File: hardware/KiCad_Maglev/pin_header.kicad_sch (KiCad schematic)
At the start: 0 parts

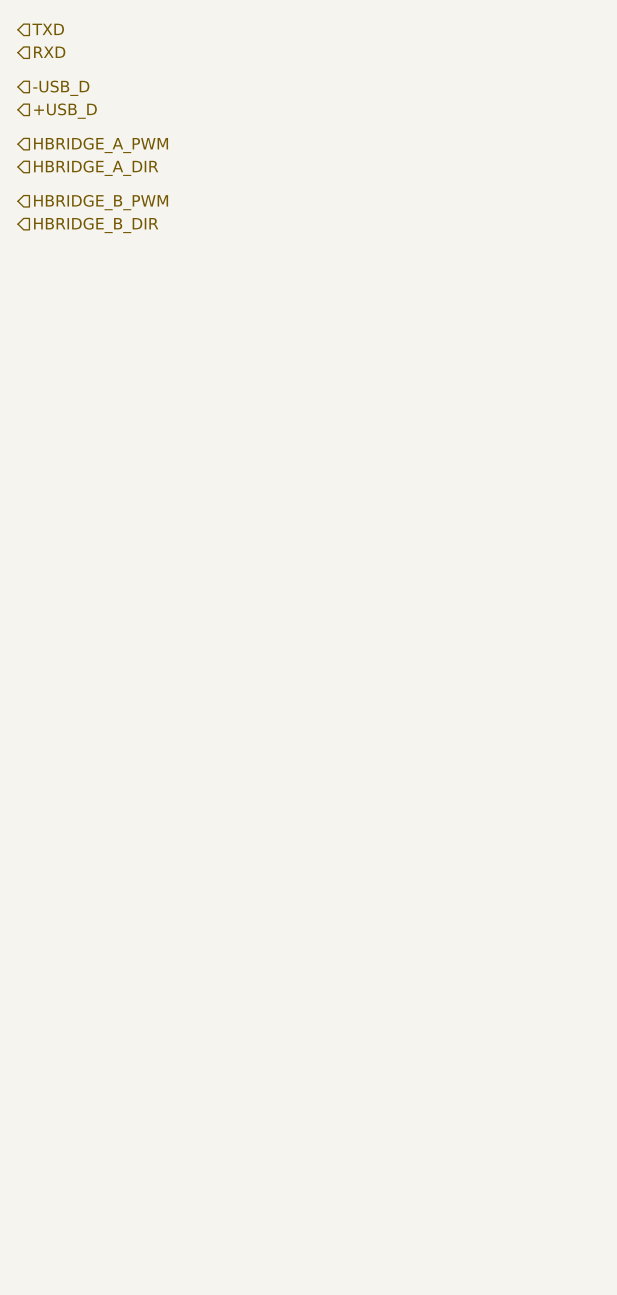
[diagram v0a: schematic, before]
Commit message: Update KiCad schematic sheets
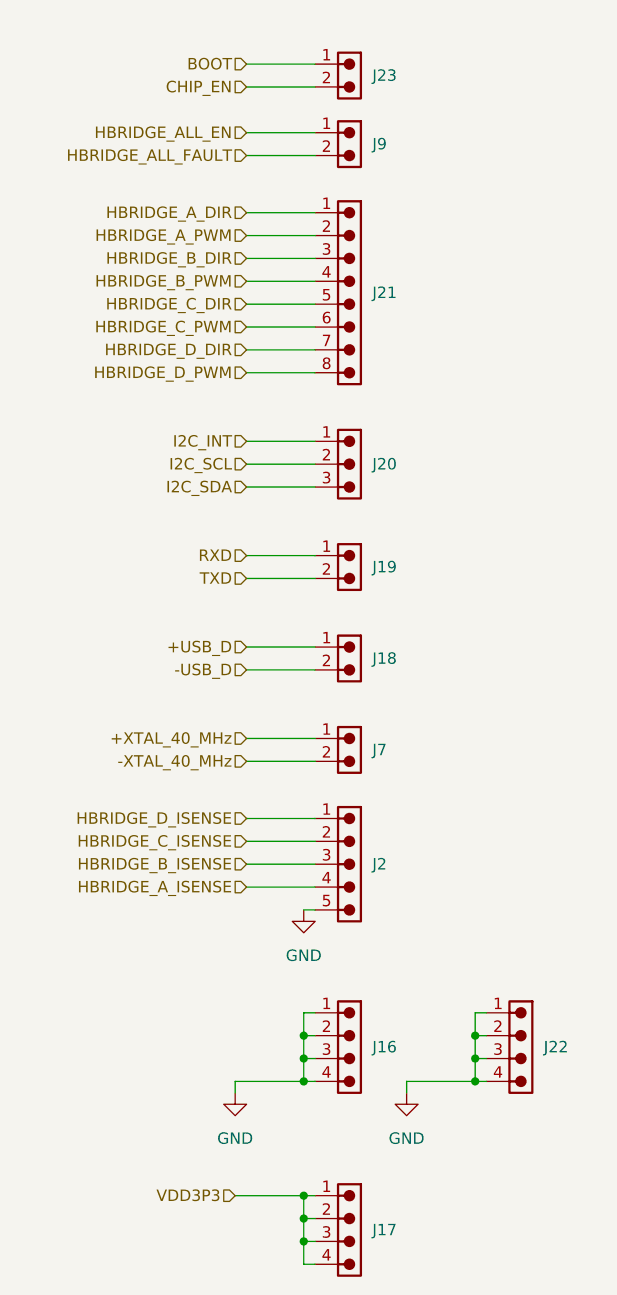
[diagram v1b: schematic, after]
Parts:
- added J16, J17, J22: 61300411121, Connector_THT_Wurth:J_Wurth_WR-PHD_61300411121, symbol Connector_Wurth_WR-PHD:61300411121
- added J18, J19, J23, J7, J9: 61300211121, Connector_THT_Wurth:J_Wurth_WR-PHD_61300211121, symbol Connector_Wurth_WR-PHD:61300211121
- added J2: 61300511121, Connector_THT_Wurth:J_Wurth_WR-PHD_61300511121, symbol Connector_Wurth_WR-PHD:61300511121
- added J20: 61300311121, Connector_THT_Wurth:J_Wurth_WR-PHD_61300311121, symbol Connector_Wurth_WR-PHD:61300311121
- added J21: 61300811121, Connector_THT_Wurth:J_Wurth_WR-PHD_61300811121, symbol Connector_Wurth_WR-PHD:61300811121
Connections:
- net +USB_D: now also J18.1
- net -USB_D: now also J18.2
- net HBRIDGE_A_DIR: now also J21.1
- net HBRIDGE_A_PWM: now also J21.2
- net HBRIDGE_B_DIR: now also J21.3
- net HBRIDGE_B_PWM: now also J21.4
- net RXD: now also J19.1
- net TXD: now also J19.2
- new net +XTAL_40_MHz: J7.1
- new net -XTAL_40_MHz: J7.2
- new net BOOT: J23.1
- new net CHIP_EN: J23.2
- new net GND: J16.1, J16.2, J16.3, J16.4, J2.5, J22.1, J22.2, J22.3, J22.4
- new net HBRIDGE_ALL_EN: J9.1
- new net HBRIDGE_ALL_FAULT: J9.2
- new net HBRIDGE_A_ISENSE: J2.4
- new net HBRIDGE_B_ISENSE: J2.3
- new net HBRIDGE_C_DIR: J21.5
- new net HBRIDGE_C_ISENSE: J2.2
- new net HBRIDGE_C_PWM: J21.6
- new net HBRIDGE_D_DIR: J21.7
- new net HBRIDGE_D_ISENSE: J2.1
- new net HBRIDGE_D_PWM: J21.8
- new net I2C_INT: J20.1
- new net I2C_SCL: J20.2
- new net I2C_SDA: J20.3
- new net VDD3P3: J17.1, J17.2, J17.3, J17.4

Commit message: Added Footprints/Models for coil and ringmagnet, changed most components to 1206 series
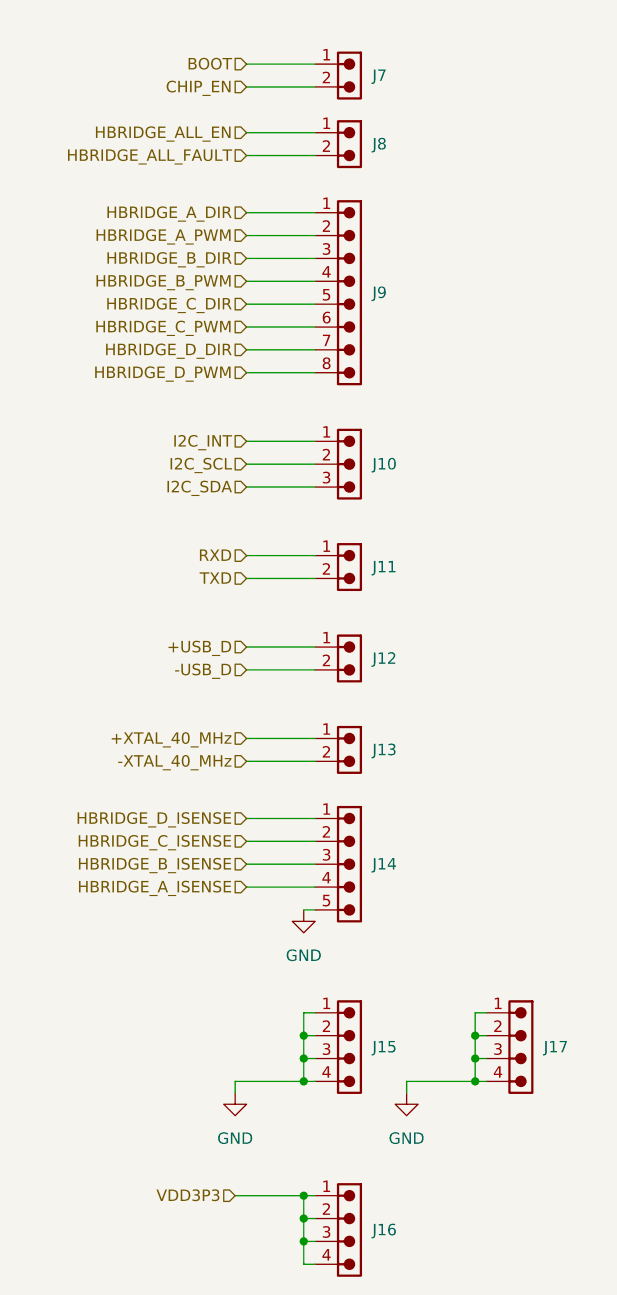
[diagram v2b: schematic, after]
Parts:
- renumbered J20 to J10, J19 to J11, J18 to J12, J7 to J13, J2 to J14, J16 to J15, J17 to J16, J22 to J17, J23 to J7, J9 to J8, J21 to J9
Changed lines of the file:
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@@
 		(dnp no)
 		(fields_autoplaced yes)
-		(property "Reference" "J23"
+		(property "Reference" "J7"
 			(at 57.15 29.2099 90)
 			(show_name no)
@@
 			(project "Maglev"
 				(path "/cf460145-35f8-4019-907e-b966a2c32625/995c9bf7-2294-48ef-9351-edb7b71be1a3"
-					(reference "J23")
+					(reference "J7")
 					(unit 1)
 				)
@@
 		(dnp no)
 		(fields_autoplaced yes)
-		(property "Reference" "J7"
+		(property "Reference" "J13"
 			(at 57.15 104.1399 90)
 			(show_name no)
@@
 			(project "Maglev"
 				(path "/cf460145-35f8-4019-907e-b966a2c32625/995c9bf7-2294-48ef-9351-edb7b71be1a3"
-					(reference "J7")
+					(reference "J13")
 					(unit 1)
 				)
@@
 		(dnp no)
 		(fields_autoplaced yes)
-		(property "Reference" "#PWR037"
+		(property "Reference" "#PWR042"
 			(at 49.53 128.27 0)
 			(hide yes)
@@
 			(project "Maglev"
 				(path "/cf460145-35f8-4019-907e-b966a2c32625/995c9bf7-2294-48ef-9351-edb7b71be1a3"
-					(reference "#PWR037")
+					(reference "#PWR042")
 					(unit 1)
 				)
@@
 		(dnp no)
 		(fields_autoplaced yes)
-		(property "Reference" "J19"
+		(property "Reference" "J11"
 			(at 57.15 83.8199 90)
 			(show_name no)
@@
 			(project "Maglev"
 				(path "/cf460145-35f8-4019-907e-b966a2c32625/995c9bf7-2294-48ef-9351-edb7b71be1a3"
-					(reference "J19")
+					(reference "J11")
 					(unit 1)
 				)
@@
 		(dnp no)
 		(fields_autoplaced yes)
-		(property "Reference" "#PWR041"
+		(property "Reference" "#PWR043"
 			(at 60.96 148.59 0)
 			(hide yes)
@@
 			(project "Maglev"
 				(path "/cf460145-35f8-4019-907e-b966a2c32625/995c9bf7-2294-48ef-9351-edb7b71be1a3"
-					(reference "#PWR041")
+					(reference "#PWR043")
 					(unit 1)
 				)
@@
 		(dnp no)
 		(fields_autoplaced yes)
-		(property "Reference" "#PWR040"
+		(property "Reference" "#PWR041"
 			(at 41.91 148.59 0)
 			(hide yes)
@@
 			(project "Maglev"
 				(path "/cf460145-35f8-4019-907e-b966a2c32625/995c9bf7-2294-48ef-9351-edb7b71be1a3"
-					(reference "#PWR040")
+					(reference "#PWR041")
 					(unit 1)
 				)
@@
 		(dnp no)
 		(fields_autoplaced yes)
-		(property "Reference" "J21"
+		(property "Reference" "J9"
 			(at 57.15 53.3399 90)
 			(show_name no)
@@
 			(project "Maglev"
 				(path "/cf460145-35f8-4019-907e-b966a2c32625/995c9bf7-2294-48ef-9351-edb7b71be1a3"
-					(reference "J21")
+					(reference "J9")
 					(unit 1)
 				)
@@
 		(dnp no)
 		(fields_autoplaced yes)
-		(property "Reference" "J22"
+		(property "Reference" "J17"
 			(at 76.2 137.1599 90)
 			(show_name no)
@@
 			(project "Maglev"
 				(path "/cf460145-35f8-4019-907e-b966a2c32625/995c9bf7-2294-48ef-9351-edb7b71be1a3"
-					(reference "J22")
+					(reference "J17")
 					(unit 1)
 				)
@@
 		(dnp no)
 		(fields_autoplaced yes)
-		(property "Reference" "J2"
+		(property "Reference" "J14"
 			(at 57.15 116.8399 90)
 			(show_name no)
@@
 			(project "Maglev"
 				(path "/cf460145-35f8-4019-907e-b966a2c32625/995c9bf7-2294-48ef-9351-edb7b71be1a3"
-					(reference "J2")
+					(reference "J14")
 					(unit 1)
 				)
@@
 		(dnp no)
 		(fields_autoplaced yes)
-		(property "Reference" "J17"
+		(property "Reference" "J16"
 			(at 57.15 157.4799 90)
 			(show_name no)
@@
 			(project "Maglev"
 				(path "/cf460145-35f8-4019-907e-b966a2c32625/995c9bf7-2294-48ef-9351-edb7b71be1a3"
-					(reference "J17")
+					(reference "J16")
 					(unit 1)
 				)
@@
 		(dnp no)
 		(fields_autoplaced yes)
-		(property "Reference" "J9"
+		(property "Reference" "J8"
 			(at 57.15 36.8299 90)
 			(show_name no)
@@
 			(project "Maglev"
 				(path "/cf460145-35f8-4019-907e-b966a2c32625/995c9bf7-2294-48ef-9351-edb7b71be1a3"
-					(reference "J9")
+					(reference "J8")
 					(unit 1)
 				)
@@
 		(dnp no)
 		(fields_autoplaced yes)
-		(property "Reference" "J16"
+		(property "Reference" "J15"
 			(at 57.15 137.1599 90)
 			(show_name no)
@@
 			(project "Maglev"
 				(path "/cf460145-35f8-4019-907e-b966a2c32625/995c9bf7-2294-48ef-9351-edb7b71be1a3"
-					(reference "J16")
+					(reference "J15")
 					(unit 1)
 				)
@@
 		(dnp no)
 		(fields_autoplaced yes)
-		(property "Reference" "J18"
+		(property "Reference" "J12"
 			(at 57.15 93.9799 90)
 			(show_name no)
@@
 			(project "Maglev"
 				(path "/cf460145-35f8-4019-907e-b966a2c32625/995c9bf7-2294-48ef-9351-edb7b71be1a3"
-					(reference "J18")
+					(reference "J12")
 					(unit 1)
 				)
@@
 		(dnp no)
 		(fields_autoplaced yes)
-		(property "Reference" "J20"
+		(property "Reference" "J10"
 			(at 57.15 72.3899 90)
 			(show_name no)
@@
 			(project "Maglev"
 				(path "/cf460145-35f8-4019-907e-b966a2c32625/995c9bf7-2294-48ef-9351-edb7b71be1a3"
-					(reference "J20")
+					(reference "J10")
 					(unit 1)
 				)

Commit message: changed mounting and spacing system and  some detail changes
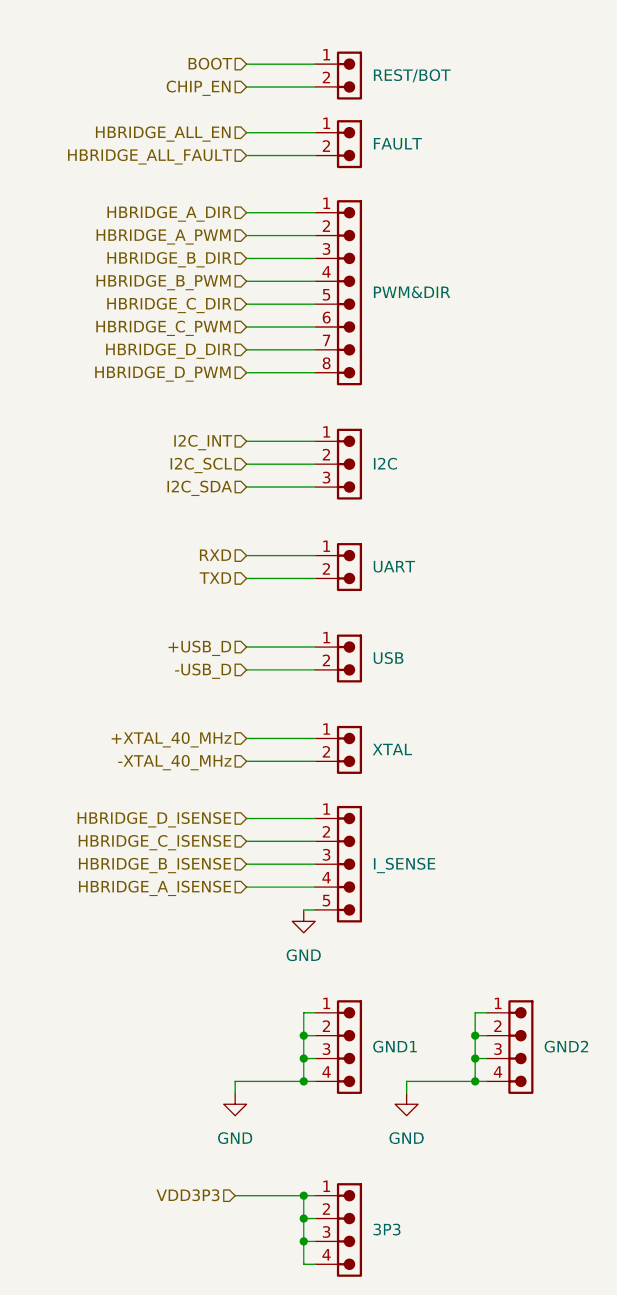
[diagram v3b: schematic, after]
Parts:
- renumbered J16 to 3P3, J8 to FAULT, J15 to GND1, J17 to GND2, J10 to I2C, J14 to I_SENSE, J9 to PWM&DIR, J7 to REST/BOT, J11 to UART, J12 to USB, J13 to XTAL
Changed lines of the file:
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@@
 		(dnp no)
 		(fields_autoplaced yes)
-		(property "Reference" "J7"
+		(property "Reference" "REST/BOT"
 			(at 57.15 29.2099 90)
 			(show_name no)
@@
 			(project "Maglev"
 				(path "/cf460145-35f8-4019-907e-b966a2c32625/995c9bf7-2294-48ef-9351-edb7b71be1a3"
-					(reference "J7")
+					(reference "REST/BOT")
 					(unit 1)
 				)
@@
 		(dnp no)
 		(fields_autoplaced yes)
-		(property "Reference" "J13"
+		(property "Reference" "XTAL"
 			(at 57.15 104.1399 90)
 			(show_name no)
@@
 			(project "Maglev"
 				(path "/cf460145-35f8-4019-907e-b966a2c32625/995c9bf7-2294-48ef-9351-edb7b71be1a3"
-					(reference "J13")
+					(reference "XTAL")
 					(unit 1)
 				)
@@
 		(dnp no)
 		(fields_autoplaced yes)
-		(property "Reference" "J11"
+		(property "Reference" "UART"
 			(at 57.15 83.8199 90)
 			(show_name no)
@@
 			(project "Maglev"
 				(path "/cf460145-35f8-4019-907e-b966a2c32625/995c9bf7-2294-48ef-9351-edb7b71be1a3"
-					(reference "J11")
+					(reference "UART")
 					(unit 1)
 				)
@@
 		(dnp no)
 		(fields_autoplaced yes)
-		(property "Reference" "J9"
+		(property "Reference" "PWM&DIR"
 			(at 57.15 53.3399 90)
 			(show_name no)
@@
 			(project "Maglev"
 				(path "/cf460145-35f8-4019-907e-b966a2c32625/995c9bf7-2294-48ef-9351-edb7b71be1a3"
-					(reference "J9")
+					(reference "PWM&DIR")
 					(unit 1)
 				)
@@
 		(dnp no)
 		(fields_autoplaced yes)
-		(property "Reference" "J17"
+		(property "Reference" "GND2"
 			(at 76.2 137.1599 90)
 			(show_name no)
@@
 			(project "Maglev"
 				(path "/cf460145-35f8-4019-907e-b966a2c32625/995c9bf7-2294-48ef-9351-edb7b71be1a3"
-					(reference "J17")
+					(reference "GND2")
 					(unit 1)
 				)
@@
 		(dnp no)
 		(fields_autoplaced yes)
-		(property "Reference" "J14"
+		(property "Reference" "I_SENSE"
 			(at 57.15 116.8399 90)
 			(show_name no)
@@
 			(project "Maglev"
 				(path "/cf460145-35f8-4019-907e-b966a2c32625/995c9bf7-2294-48ef-9351-edb7b71be1a3"
-					(reference "J14")
+					(reference "I_SENSE")
 					(unit 1)
 				)
@@
 		(dnp no)
 		(fields_autoplaced yes)
-		(property "Reference" "J16"
+		(property "Reference" "3P3"
 			(at 57.15 157.4799 90)
 			(show_name no)
@@
 			(project "Maglev"
 				(path "/cf460145-35f8-4019-907e-b966a2c32625/995c9bf7-2294-48ef-9351-edb7b71be1a3"
-					(reference "J16")
+					(reference "3P3")
 					(unit 1)
 				)
@@
 		(dnp no)
 		(fields_autoplaced yes)
-		(property "Reference" "J8"
+		(property "Reference" "FAULT"
 			(at 57.15 36.8299 90)
 			(show_name no)
@@
 			(project "Maglev"
 				(path "/cf460145-35f8-4019-907e-b966a2c32625/995c9bf7-2294-48ef-9351-edb7b71be1a3"
-					(reference "J8")
+					(reference "FAULT")
 					(unit 1)
 				)
@@
 		(dnp no)
 		(fields_autoplaced yes)
-		(property "Reference" "J15"
+		(property "Reference" "GND1"
 			(at 57.15 137.1599 90)
 			(show_name no)
@@
 			(project "Maglev"
 				(path "/cf460145-35f8-4019-907e-b966a2c32625/995c9bf7-2294-48ef-9351-edb7b71be1a3"
-					(reference "J15")
+					(reference "GND1")
 					(unit 1)
 				)
@@
 		(dnp no)
 		(fields_autoplaced yes)
-		(property "Reference" "J12"
+		(property "Reference" "USB"
 			(at 57.15 93.9799 90)
 			(show_name no)
@@
 			(project "Maglev"
 				(path "/cf460145-35f8-4019-907e-b966a2c32625/995c9bf7-2294-48ef-9351-edb7b71be1a3"
-					(reference "J12")
+					(reference "USB")
 					(unit 1)
 				)
@@
 		(dnp no)
 		(fields_autoplaced yes)
-		(property "Reference" "J10"
+		(property "Reference" "I2C"
 			(at 57.15 72.3899 90)
 			(show_name no)
@@
 			(project "Maglev"
 				(path "/cf460145-35f8-4019-907e-b966a2c32625/995c9bf7-2294-48ef-9351-edb7b71be1a3"
-					(reference "J10")
+					(reference "I2C")
 					(unit 1)
 				)

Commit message: Route power PCB and implement board-to-board connector
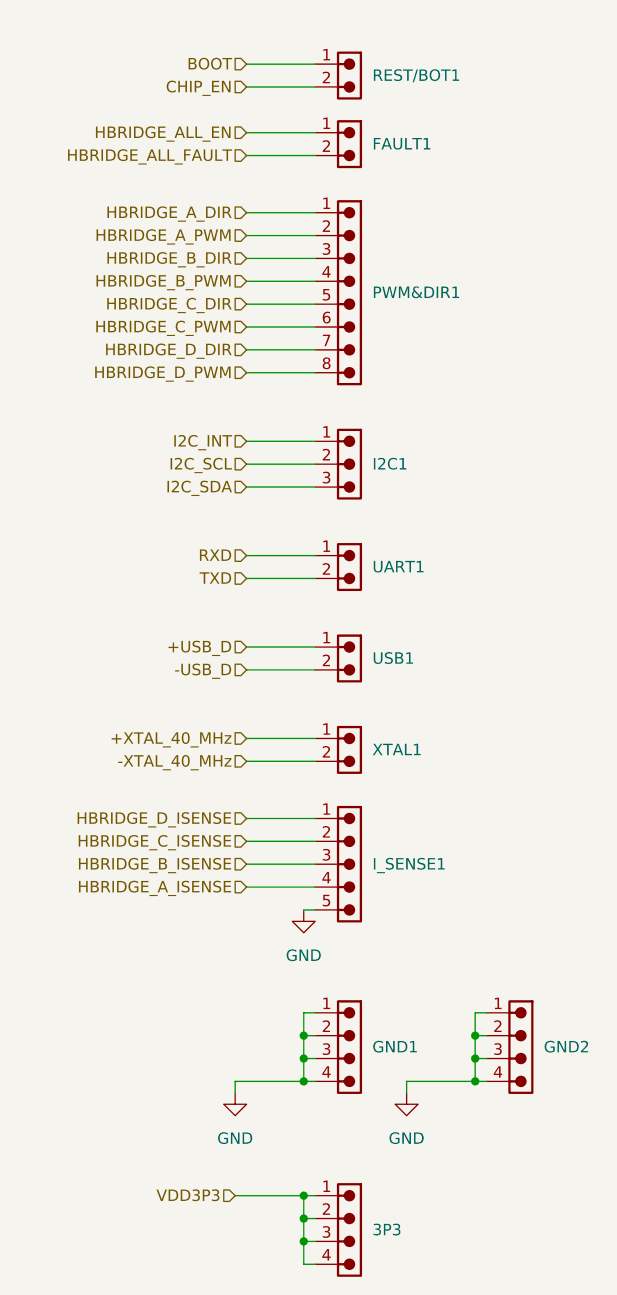
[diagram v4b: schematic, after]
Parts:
- renumbered FAULT to FAULT1, I2C to I2C1, I_SENSE to I_SENSE1, PWM&DIR to PWM&DIR1, REST/BOT to REST/BOT1, UART to UART1, USB to USB1, XTAL to XTAL1
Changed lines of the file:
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@@
 		(dnp no)
 		(fields_autoplaced yes)
-		(property "Reference" "REST/BOT"
+		(property "Reference" "REST/BOT1"
 			(at 57.15 29.2099 90)
 			(show_name no)
@@
 			(project "Maglev"
 				(path "/cf460145-35f8-4019-907e-b966a2c32625/995c9bf7-2294-48ef-9351-edb7b71be1a3"
-					(reference "REST/BOT")
+					(reference "REST/BOT1")
 					(unit 1)
 				)
@@
 		(dnp no)
 		(fields_autoplaced yes)
-		(property "Reference" "XTAL"
+		(property "Reference" "XTAL1"
 			(at 57.15 104.1399 90)
 			(show_name no)
@@
 			(project "Maglev"
 				(path "/cf460145-35f8-4019-907e-b966a2c32625/995c9bf7-2294-48ef-9351-edb7b71be1a3"
-					(reference "XTAL")
+					(reference "XTAL1")
 					(unit 1)
 				)
@@
 		(dnp no)
 		(fields_autoplaced yes)
-		(property "Reference" "UART"
+		(property "Reference" "UART1"
 			(at 57.15 83.8199 90)
 			(show_name no)
@@
 			(project "Maglev"
 				(path "/cf460145-35f8-4019-907e-b966a2c32625/995c9bf7-2294-48ef-9351-edb7b71be1a3"
-					(reference "UART")
+					(reference "UART1")
 					(unit 1)
 				)
@@
 		(dnp no)
 		(fields_autoplaced yes)
-		(property "Reference" "PWM&DIR"
+		(property "Reference" "PWM&DIR1"
 			(at 57.15 53.3399 90)
 			(show_name no)
@@
 			(project "Maglev"
 				(path "/cf460145-35f8-4019-907e-b966a2c32625/995c9bf7-2294-48ef-9351-edb7b71be1a3"
-					(reference "PWM&DIR")
+					(reference "PWM&DIR1")
 					(unit 1)
 				)
@@
 		(dnp no)
 		(fields_autoplaced yes)
-		(property "Reference" "I_SENSE"
+		(property "Reference" "I_SENSE1"
 			(at 57.15 116.8399 90)
 			(show_name no)
@@
 			(project "Maglev"
 				(path "/cf460145-35f8-4019-907e-b966a2c32625/995c9bf7-2294-48ef-9351-edb7b71be1a3"
-					(reference "I_SENSE")
+					(reference "I_SENSE1")
 					(unit 1)
 				)
@@
 		(dnp no)
 		(fields_autoplaced yes)
-		(property "Reference" "FAULT"
+		(property "Reference" "FAULT1"
 			(at 57.15 36.8299 90)
 			(show_name no)
@@
 			(project "Maglev"
 				(path "/cf460145-35f8-4019-907e-b966a2c32625/995c9bf7-2294-48ef-9351-edb7b71be1a3"
-					(reference "FAULT")
+					(reference "FAULT1")
 					(unit 1)
 				)
@@
 		(dnp no)
 		(fields_autoplaced yes)
-		(property "Reference" "USB"
+		(property "Reference" "USB1"
 			(at 57.15 93.9799 90)
 			(show_name no)
@@
 			(project "Maglev"
 				(path "/cf460145-35f8-4019-907e-b966a2c32625/995c9bf7-2294-48ef-9351-edb7b71be1a3"
-					(reference "USB")
+					(reference "USB1")
 					(unit 1)
 				)
@@
 		(dnp no)
 		(fields_autoplaced yes)
-		(property "Reference" "I2C"
+		(property "Reference" "I2C1"
 			(at 57.15 72.3899 90)
 			(show_name no)
@@
 			(project "Maglev"
 				(path "/cf460145-35f8-4019-907e-b966a2c32625/995c9bf7-2294-48ef-9351-edb7b71be1a3"
-					(reference "I2C")
+					(reference "I2C1")
 					(unit 1)
 				)
